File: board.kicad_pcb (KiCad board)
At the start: 6 copper layers, 223.5 x 115 mm, 148 parts, among them J1 Conn_01x04, J10 878311420, J11 Conn_01x02, J2 Conn_2Rows-33Pins, J3 Conn_2Rows-33Pins, J4 Conn_2Rows-33Pins, J5 Conn_2Rows-33Pins, J6 Conn_2Rows-33Pins, J7 Conn_2Rows-33Pins, J8 Conn_01x04, J9 Conn_01x04, U1 MC68060RC50, U10 74LVC162245ADGG, U11 74LVC162245ADGG, U12 SIT2001BI-S2-33E-50.000000G, U13 74LVC162245ADGG, U14 SC16IS762IPW, U15 CH9350, U16 AP2161W, U17 AP2161W, U18 TPS3808DBV, U19 PCA9515AD, U2 LCMXO2-7000HC-6TG144I, U20 74LVC162245ADGG, U21 74LVC162245ADGG, U3 MR5A16AYS35, U4 IS61WV204816BLL-10TLI, U5 IS61WV204816BLL-10TLI, U6 MR5A16AYS35, U7 74LVC162245ADGG, U8 74LVC162245ADGG, U9 74LVC162245ADGG, Y1 1.8432 MHz

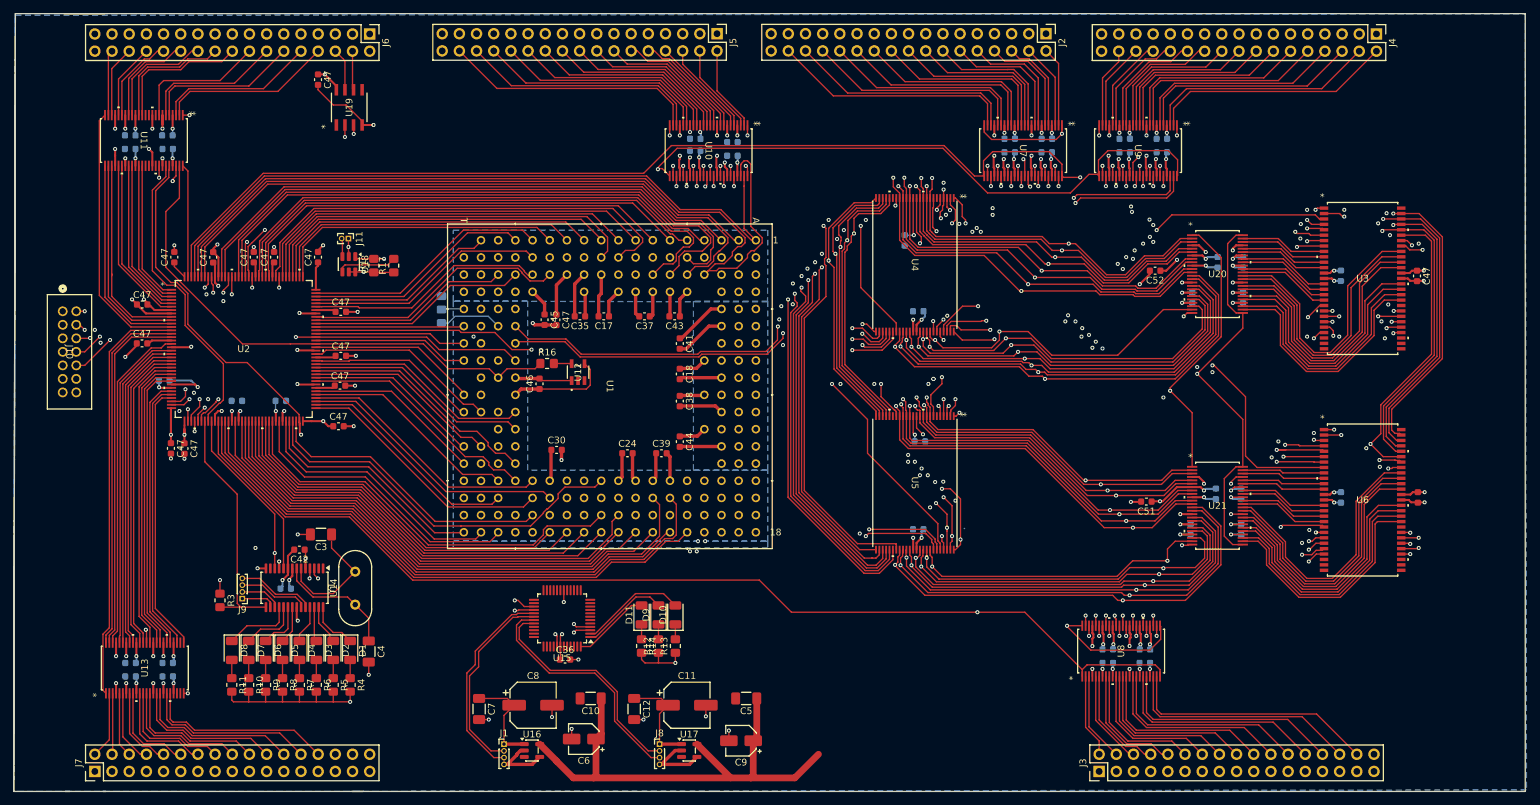
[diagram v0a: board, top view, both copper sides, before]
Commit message: Added daminping resistors
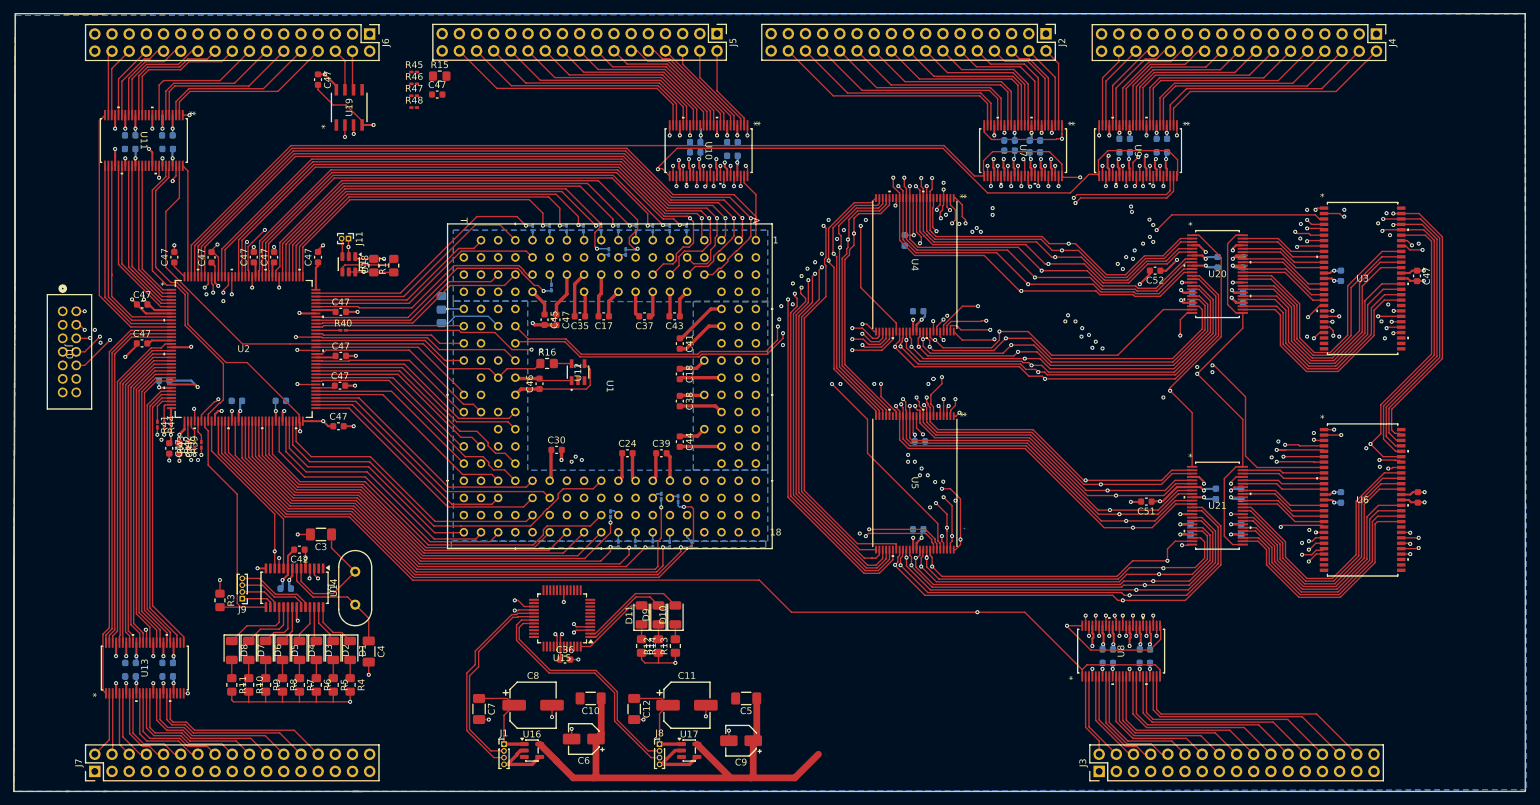
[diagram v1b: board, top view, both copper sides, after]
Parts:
- added C47: 100nF, Capacitor_SMD:C_0603_1608Metric, F.Cu at (107.6, 50.2)
- added R15: 0R, Resistor_SMD:R_0805_2012Metric_Pad1.20x1.40mm_HandSolder, F.Cu at (108.0, 47.5)
- added R18: 33R, Resistor_SMD:R_0201_0603Metric_Pad0.64x0.40mm_HandSolder, B.Cu at (143.2, 110.0)
- added R19: 33R, Resistor_SMD:R_0201_0603Metric_Pad0.64x0.40mm_HandSolder, B.Cu at (142.0, 116.8)
- added R20: 33R, Resistor_SMD:R_0201_0603Metric_Pad0.64x0.40mm_HandSolder, B.Cu at (140.8, 109.7)
- added R21: 33R, Resistor_SMD:R_0201_0603Metric_Pad0.64x0.40mm_HandSolder, B.Cu at (145.2, 116.8)
- added R22: 33R, Resistor_SMD:R_0201_0603Metric_Pad0.64x0.40mm_HandSolder, B.Cu at (139.5, 116.7)
- added R23: 33R, Resistor_SMD:R_0201_0603Metric_Pad0.64x0.40mm_HandSolder, B.Cu at (136.9, 116.6)
- added R24: 33R, Resistor_SMD:R_0201_0603Metric_Pad0.64x0.40mm_HandSolder, B.Cu at (133.2, 112.2)
- added R25: 33R, Resistor_SMD:R_0201_0603Metric_Pad0.64x0.40mm_HandSolder, B.Cu at (134.4, 116.7)
- added R26: 33R, Resistor_SMD:R_0201_0603Metric_Pad0.64x0.40mm_HandSolder, B.Cu at (142.0, 70.0)
- added R27: 33R, Resistor_SMD:R_0201_0603Metric_Pad0.64x0.40mm_HandSolder, B.Cu at (139.5, 70.0)
- added R28: 33R, Resistor_SMD:R_0201_0603Metric_Pad0.64x0.40mm_HandSolder, B.Cu at (137.0, 70.0)
- added R29: 33R, Resistor_SMD:R_0201_0603Metric_Pad0.64x0.40mm_HandSolder, B.Cu at (134.4, 70.0)
- added R30: 33R, Resistor_SMD:R_0201_0603Metric_Pad0.64x0.40mm_HandSolder, B.Cu at (135.5, 73.5)
- added R31: 33R, Resistor_SMD:R_0201_0603Metric_Pad0.64x0.40mm_HandSolder, B.Cu at (131.9, 70.0)
- added R32: 33R, Resistor_SMD:R_0201_0603Metric_Pad0.64x0.40mm_HandSolder, B.Cu at (133.0, 73.5)
- added R33: 33R, Resistor_SMD:R_0201_0603Metric_Pad0.64x0.40mm_HandSolder, B.Cu at (129.2, 70.0)
- added R34: 33R, Resistor_SMD:R_0201_0603Metric_Pad0.64x0.40mm_HandSolder, B.Cu at (144.5, 70.0)
- added R35: 33R, Resistor_SMD:R_0201_0603Metric_Pad0.64x0.40mm_HandSolder, B.Cu at (126.8, 70.0)
- added R36: 33R, Resistor_SMD:R_0201_0603Metric_Pad0.64x0.40mm_HandSolder, B.Cu at (124.2, 70.0)
- added R37: 33R, Resistor_SMD:R_0201_0603Metric_Pad0.64x0.40mm_HandSolder, B.Cu at (124.5, 78.8)
- added R38: 33R, Resistor_SMD:R_0201_0603Metric_Pad0.64x0.40mm_HandSolder, B.Cu at (121.8, 70.0)
- added R39: 33R, Resistor_SMD:R_0201_0603Metric_Pad0.64x0.40mm_HandSolder, F.Cu at (72.8, 102.0)
- added R40: 22R, Resistor_SMD:R_0201_0603Metric_Pad0.64x0.40mm_HandSolder, F.Cu at (93.7, 85.1)
- added R41: 22R, Resistor_SMD:R_0201_0603Metric_Pad0.64x0.40mm_HandSolder, F.Cu at (66.2, 99.0)
- added R42: 22R, Resistor_SMD:R_0201_0603Metric_Pad0.64x0.40mm_HandSolder, F.Cu at (71.8, 102.0)
- added R43: 33R, Resistor_SMD:R_0201_0603Metric_Pad0.64x0.40mm_HandSolder, F.Cu at (70.8, 102.0)
- added R44: 33R, Resistor_SMD:R_0201_0603Metric_Pad0.64x0.40mm_HandSolder, F.Cu at (67.2, 99.0)
- added R45: 33R, Resistor_SMD:R_0201_0603Metric_Pad0.64x0.40mm_HandSolder, F.Cu at (104.2, 46.9)
- added R46: 33R, Resistor_SMD:R_0201_0603Metric_Pad0.64x0.40mm_HandSolder, F.Cu at (104.2, 48.6)
- added R47: 33R, Resistor_SMD:R_0201_0603Metric_Pad0.64x0.40mm_HandSolder, F.Cu at (104.2, 50.4)
- added R48: 33R, Resistor_SMD:R_0201_0603Metric_Pad0.64x0.40mm_HandSolder, F.Cu at (104.2, 52.1)
- R16: value 0R -> 22R
- moved C2 1.79 mm to (196.0, 57.0), turned to 180 degrees
- moved C19 1.75 mm to (192.2, 57.0)
- moved C25 1.75 mm to (192.2, 58.5)
- moved C1 1.75 mm to (196.0, 58.8), turned to 180 degrees
- moved C47 0.75 mm to (69.5, 102.5)
- moved C16 0.50 mm to (145.8, 57.2)
- moved C15 0.25 mm to (145.8, 58.8)
- moved C47 0.25 mm to (68.0, 102.5)
- moved C47 0.25 mm to (74.2, 74.3)
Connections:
- U1 pad Q4: /BS0 -> /BS0_INT
- U1 pad Q5: /BS1 -> /BS1_INT
- U1 pad Q6: /BS2 -> /BS2_INT
- U1 pad Q7: /BS3 -> /BS3_INT
- U10 pad 26: /A16 -> /AR16
- U10 pad 27: /A17 -> /AR17
- U10 pad 29: /A18 -> /AR18
- U10 pad 30: /A19 -> /AR19
- U10 pad 32: /A20 -> /AR20
- U10 pad 33: /A21 -> /AR21
- U10 pad 35: /A22 -> /AR22
- U2 pad 100: /A11 -> /AR11
- U2 pad 107: /A10 -> /AR10
- U2 pad 109: /A12 -> /AR12
- U2 pad 110: /A13 -> /AR13
- U2 pad 111: /A14 -> /AR14
- U2 pad 112: /A15 -> /AR15
- U2 pad 113: /A16 -> /AR16
- U2 pad 114: /A17 -> /AR17
- U2 pad 115: /A18 -> /AR18
- U2 pad 117: /A19 -> /AR19
- U2 pad 119: /A20 -> /AR20
- U2 pad 120: /A21 -> /AR21
- U2 pad 121: /A22 -> /AR22
- U2 pad 34: /EPROM_OE -> /EPROM_OE_INT
- U2 pad 35: /EPROM_CS -> /EPROM_CS_INT
- U2 pad 38: /RAM_CS -> /RAM_CS_INT
- U2 pad 39: /RAM_OE -> /RAM_OE_INT
- U2 pad 41: /RW -> /RW_INT
- U2 pad 49: /A8 -> /AR9
- U2 pad 50: /A9 -> /AR8
- U2 pad 52: /A7 -> /AR7
- U2 pad 54: /A6 -> /AR6
- U2 pad 55: /A5 -> /AR5
- U2 pad 56: /A4 -> /AR4
- U2 pad 57: /A3 -> /AR3
- U2 pad 58: /A2 -> /AR2
- U2 pad 96: /EPROM_BUFFER_OE -> /EPROM_BUFFER_OE_INT
- U3 pad 1: /A22 -> /AR22
- U3 pad 2: /A21 -> /AR21
- U3 pad 20: /A7 -> /AR7
- U3 pad 21: /A8 -> /AR8
- U3 pad 22: /A9 -> /AR9
- U3 pad 23: /A10 -> /AR10
- U3 pad 24: /A11 -> /AR11
- U3 pad 3: /A2 -> /AR2
- U3 pad 31: /A12 -> /AR12
- U3 pad 32: /A13 -> /AR13
- U3 pad 33: /A14 -> /AR14
- U3 pad 34: /A15 -> /AR15
- U3 pad 35: /A16 -> /AR16
- U3 pad 4: /A3 -> /AR3
- U3 pad 5: /A4 -> /AR4
- U3 pad 50: /A17 -> /AR17
- U3 pad 51: /A18 -> /AR18
- U3 pad 52: /A19 -> /AR19
- U3 pad 53: /A20 -> /AR20
- U3 pad 6: /A5 -> /AR5
- U3 pad 7: /A6 -> /AR6
- U4 pad 1: /A6 -> /AR6
- U4 pad 2: /A5 -> /AR5
- U4 pad 20: /A21 -> /AR21
- U4 pad 21: /A20 -> /AR20
- U4 pad 22: /A19 -> /AR19
- U4 pad 23: /A18 -> /AR18
- U4 pad 24: /A17 -> /AR17
- U4 pad 25: /A16 -> /AR16
- U4 pad 26: /A15 -> /AR15
- U4 pad 27: /A14 -> /AR14
- U4 pad 28: /A13 -> /AR13
- U4 pad 29: /A12 -> /AR12
- U4 pad 3: /A4 -> /AR4
- U4 pad 30: /A11 -> /AR11
- U4 pad 31: /A22 -> /AR22
- U4 pad 4: /A3 -> /AR3
- U4 pad 45: /A10 -> /AR10
- U4 pad 46: /A9 -> /AR9
- U4 pad 47: /A8 -> /AR8
- U4 pad 48: /A7 -> /AR7
- U4 pad 5: /A2 -> /AR2
- U5 pad 1: /A6 -> /AR6
- U5 pad 2: /A5 -> /AR5
- U5 pad 20: /A21 -> /AR21
- U5 pad 21: /A20 -> /AR20
- U5 pad 22: /A19 -> /AR19
- U5 pad 23: /A18 -> /AR18
- U5 pad 24: /A17 -> /AR17
- U5 pad 25: /A16 -> /AR16
- U5 pad 26: /A15 -> /AR15
- U5 pad 27: /A14 -> /AR14
- U5 pad 28: /A13 -> /AR13
- U5 pad 29: /A12 -> /AR12
- U5 pad 3: /A4 -> /AR4
- U5 pad 30: /A11 -> /AR11
- U5 pad 31: /A22 -> /AR22
- U5 pad 4: /A3 -> /AR3
- U5 pad 45: /A10 -> /AR10
- U5 pad 46: /A9 -> /AR9
- U5 pad 47: /A8 -> /AR8
- U5 pad 48: /A7 -> /AR7
- U5 pad 5: /A2 -> /AR2
- U6 pad 1: /A22 -> /AR22
- U6 pad 2: /A21 -> /AR21
- U6 pad 20: /A7 -> /AR7
- U6 pad 21: /A8 -> /AR8
- U6 pad 22: /A9 -> /AR9
- U6 pad 23: /A10 -> /AR10
- U6 pad 24: /A11 -> /AR11
- U6 pad 3: /A2 -> /AR2
- U6 pad 31: /A12 -> /AR12
- U6 pad 32: /A13 -> /AR13
- U6 pad 33: /A14 -> /AR14
- U6 pad 34: /A15 -> /AR15
- U6 pad 35: /A16 -> /AR16
- U6 pad 4: /A3 -> /AR3
- U6 pad 5: /A4 -> /AR4
- U6 pad 50: /A17 -> /AR17
- U6 pad 51: /A18 -> /AR18
- U6 pad 52: /A19 -> /AR19
- U6 pad 53: /A20 -> /AR20
- U6 pad 6: /A5 -> /AR5
- U6 pad 7: /A6 -> /AR6
- U9 pad 26: /A15 -> /AR15
- U9 pad 27: /A14 -> /AR14
- U9 pad 29: /A13 -> /AR13
- U9 pad 30: /A12 -> /AR12
- U9 pad 32: /A11 -> /AR11
- U9 pad 33: /A10 -> /AR10
- U9 pad 35: /A9 -> /AR9
- U9 pad 36: /A8 -> /AR8
- U9 pad 37: /A7 -> /AR7
- U9 pad 38: /A6 -> /AR6
- U9 pad 40: /A5 -> /AR5
- U9 pad 41: /A4 -> /AR4
- U9 pad 43: /A3 -> /AR3
- U9 pad 44: /A2 -> /AR2
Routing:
- net /AR9: track 0.00 -> 345.2 mm, vias 0 -> 9
- net /A9: track 342.7 -> 1.32 mm, vias 8 -> 0
- net /A8: track 337.9 -> 1.76 mm, vias 8 -> 0
- net /AR8: track 0.00 -> 335.2 mm, vias 0 -> 9
- net /AR13: track 0.00 -> 331.9 mm, vias 0 -> 7
- net /AR12: track 0.00 -> 329.7 mm, vias 0 -> 7
- net /AR15: track 0.00 -> 328.7 mm, vias 0 -> 7
- net /AR7: track 0.00 -> 328.4 mm, vias 0 -> 9
- net /AR14: track 0.00 -> 327.0 mm, vias 0 -> 7
- net /A7: track 327.2 -> 1.43 mm, vias 8 -> 0
- net /AR16: track 0.00 -> 325.0 mm, vias 0 -> 6
- net /A13: track 326.0 -> 1.36 mm, vias 6 -> 0
- net /A15: track 324.4 -> 1.34 mm, vias 6 -> 0
- net /A12: track 323.3 -> 1.35 mm, vias 6 -> 0
- net /A14: track 322.0 -> 1.38 mm, vias 6 -> 0
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
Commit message: Resistors on Bs0-3 and A0, A1
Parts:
- added R49: 33R, Resistor_SMD:R_0201_0603Metric_Pad0.64x0.40mm_HandSolder, B.Cu at (129.2, 116.8)
- added R50: 33R, Resistor_SMD:R_0201_0603Metric_Pad0.64x0.40mm_HandSolder, B.Cu at (131.9, 116.8)
- R45, R46, R47, R48: moved to B.Cu
- moved R48 38.7 mm to (121.0, 87.0), turned to 180 degrees
- moved R47 38.5 mm to (120.5, 85.2), turned to 90 degrees
- moved R46 37.6 mm to (121.0, 82.2), turned to 180 degrees
- moved R45 36.7 mm to (120.5, 79.8), turned to 90 degrees
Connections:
- U2 pad 59: /A1 -> /AR1
- U2 pad 60: /A0 -> /AR0
- U9 pad 46: /A1 -> /AR1
- U9 pad 47: /A0 -> /AR0
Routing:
- net /A1: track 202.0 -> 1.46 mm, vias 1 -> 0
- net /AR1: track 0.00 -> 199.7 mm, vias 0 -> 2
- net /AR0: track 0.00 -> 199.5 mm, vias 0 -> 2
- net /A0: track 200.4 -> 1.45 mm, vias 1 -> 0
- net /EXT_PD5: track 0.00 -> 29.0 mm
- net /BS1: track 188.6 -> 191.6 mm, vias 3 -> 4
- net /BS3: track 161.8 -> 159.7 mm, vias 3 -> 4
- net /BS0: track 193.1 -> 195.1 mm, vias 3 -> 4
- net /BS2: track 183.5 -> 181.8 mm, vias 3 -> 4
- net /BS1_INT: track 0.00 -> 1.66 mm
- net /BS2_INT: track 0.00 -> 1.48 mm
- net /BS3_INT: track 0.00 -> 1.42 mm
- net /BS0_INT: track 0.00 -> 1.33 mm
- net /AR2: track 302.1 -> 303.4 mm
